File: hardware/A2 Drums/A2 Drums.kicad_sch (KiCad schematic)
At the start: 21 parts, among them T1 2N3904

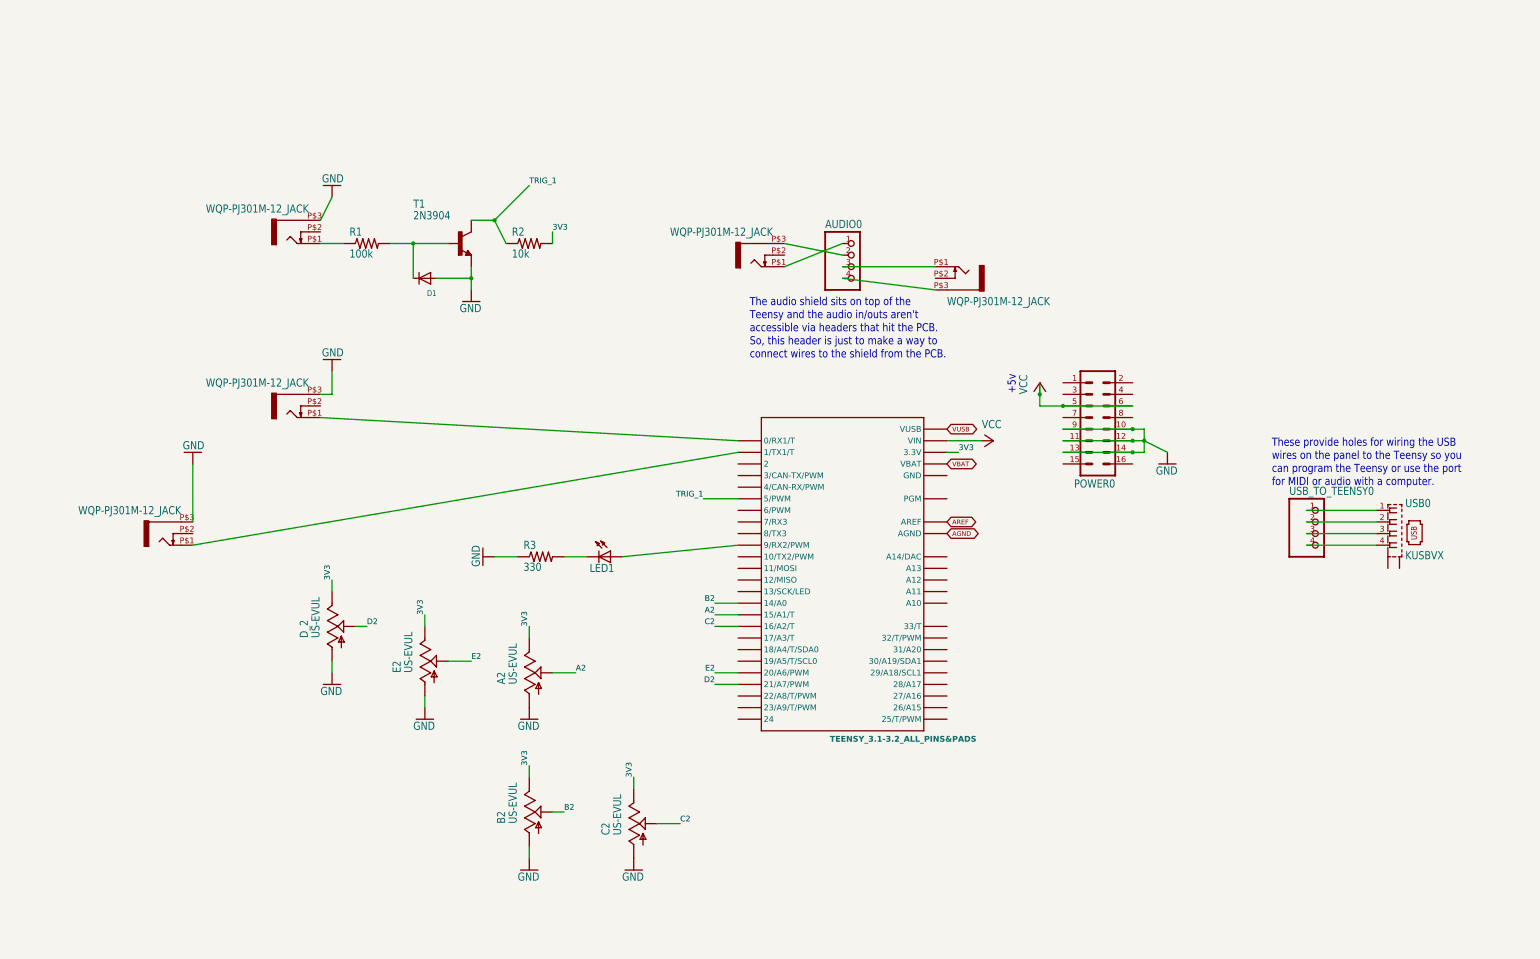
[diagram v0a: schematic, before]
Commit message: V2 of hardware and made a version of the software that uses the pt8211 chip for audio
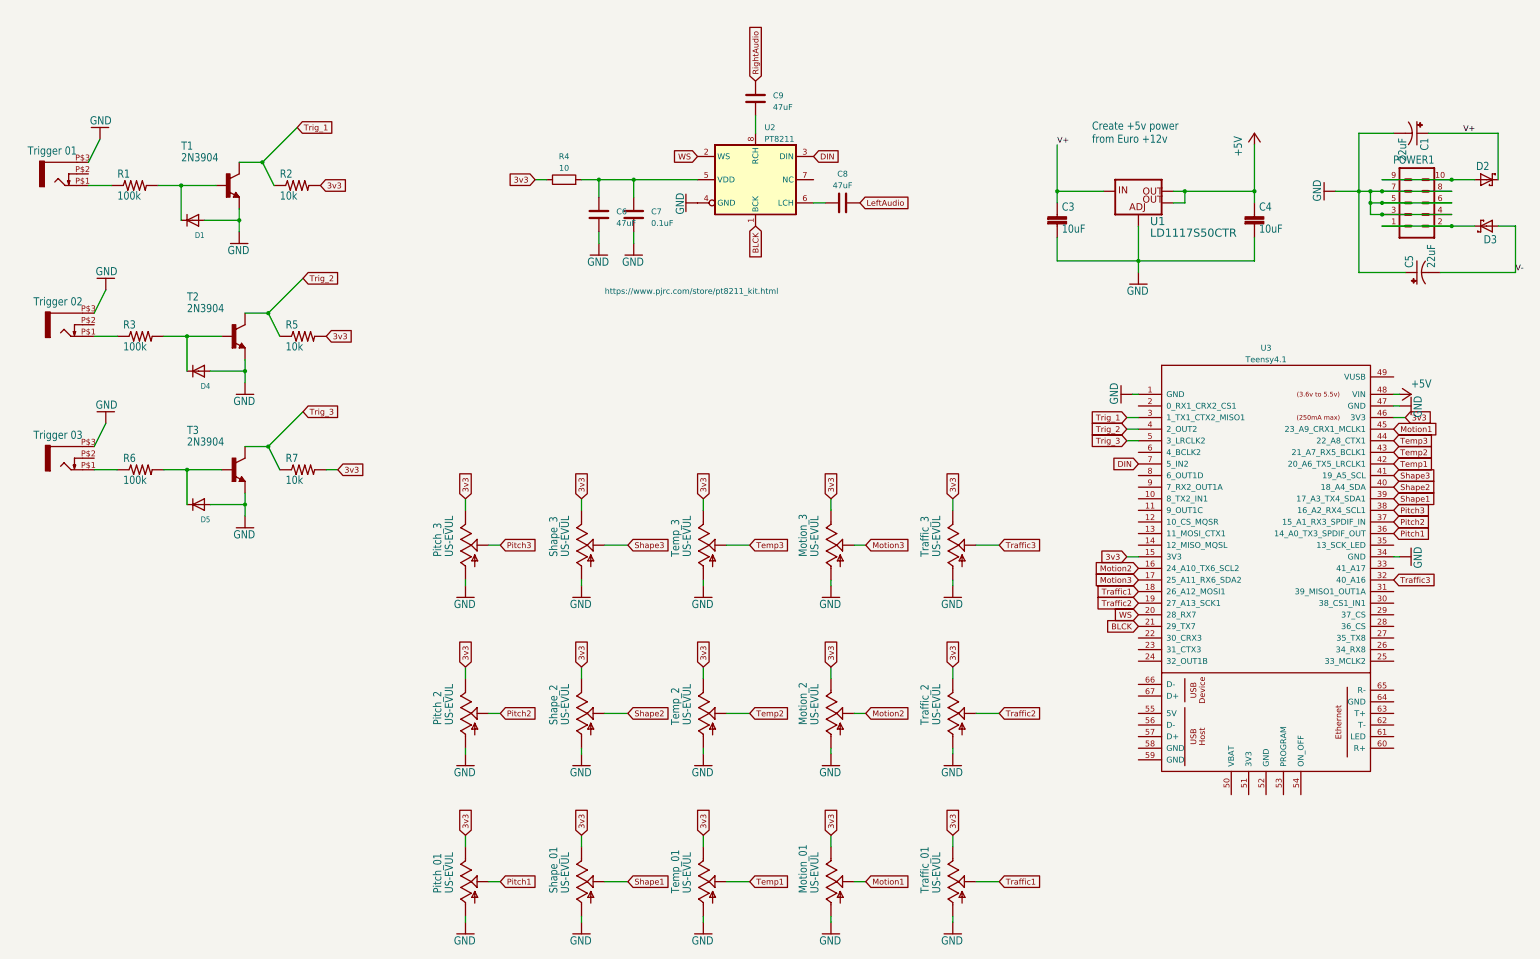
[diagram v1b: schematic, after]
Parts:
- removed AUDIO0, USB_TO_TEENSY0: PINHD-1X4, A2 Drums:1X04, symbol A2 Drums-eagle-import:PINHD-1X4
- removed AUD_IN_R0, AUD_OUT0, CD_IN0, CD_OUT0: WQP-PJ301M-12_JACK, A2 Drums:WQP-PJ301M-12_JACK, symbol A2 Drums-eagle-import:WQP-PJ301M-12_JACK
- removed LED1: LED3MM, A2 Drums:LED3MM, symbol A2 Drums-eagle-import:LED3MM
- removed POWER0: MA08-2, A2 Drums:MA08-2, symbol A2 Drums-eagle-import:MA08-2
- removed TEENSY_3.2: TEENSY_3.1-3.2_ALL_PINS&PADS, A2 Drums:TEENSY_3.0-3.2_ALL_PINS_&_PADS, symbol A2 Drums-eagle-import:TEENSY_3.1-3.2_ALL_PINS&PADS
- removed USB0: KUSBVX, A2 Drums:KUSBVX, symbol A2 Drums-eagle-import:KUSBVX
- added C1, C5: 22uF, Simple Euclidean PCB v4:E2,5-5, symbol Simple Euclidean PCB v4-eagle-import:CPOL-USE2.5-5
- added C3, C4: 10uF, Simple Euclidean PCB v4:C5B2.5, symbol Simple Euclidean PCB v4-eagle-import:C5/2.5
- added C6, C8, C9: 47uF, Capacitor_THT:C_Axial_L5.1mm_D3.1mm_P7.50mm_Horizontal, symbol Device:C
- added C7: 0.1uF, Capacitor_THT:C_Axial_L5.1mm_D3.1mm_P7.50mm_Horizontal, symbol Device:C
- added D2, D3: SCHOTTKY-DIODEDO41, Simple Euclidean PCB v4:DO41-10, symbol Simple Euclidean PCB v4-eagle-import:SCHOTTKY-DIODEDO41
- added D4, D5: DIODESOD-123, A2 Drums:SOD-123, symbol A2 Drums-eagle-import:DIODESOD-123
- added Motion_2, Motion_3, Pitch_2, Pitch_3, Shape_2, Shape_3, Temp_2, Temp_3, Traffic_2, Traffic_3: US-EVUL, A2 Drums:EVUFXL, symbol A2 Drums-eagle-import:US-EVUL
- added POWER1: MA05-2, Simple Euclidean PCB v4:MA05-2, symbol Simple Euclidean PCB v4-eagle-import:MA05-2
- added R4: 10, PCM_4ms_Resistor:R_Axial_DIN0207_L6.3mm_D2.5mm_P7.62mm_Horizontal, symbol Device:R
- added R5, R7: 10k, A2 Drums:R0805, symbol A2 Drums-eagle-import:R-US_R0805
- added R6: 100k, A2 Drums:R0805, symbol A2 Drums-eagle-import:R-US_R0805
- added T2, T3: 2N3904, A2 Drums:TO92, symbol A2 Drums-eagle-import:2N3904
- added TRIG2: Trigger 02, A2 Drums:WQP-PJ301M-12_JACK, symbol A2 Drums-eagle-import:WQP-PJ301M-12_JACK
- added TRIG3: Trigger 03, A2 Drums:WQP-PJ301M-12_JACK, symbol A2 Drums-eagle-import:WQP-PJ301M-12_JACK
- added U1: LD1117S50CTR, Simple Euclidean PCB v4:SOT223, symbol Simple Euclidean PCB v4-eagle-import:V_REG_LM1117SOT223
- added U2: PT8211, Package_SO:VSSOP-8_3.0x3.0mm_P0.65mm, symbol Timer:TLC555xPS
- added U3: Teensy4.1, symbol teensy:Teensy4.1
- R3: value 330 -> 100k
- TRIG1: value WQP-PJ301M-12_JACK -> Trigger 01
- renumbered B2 to Motion_01, D_2 to Pitch_01, E2 to Shape_01, A2 to Temp_01, C2 to Traffic_01
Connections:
- net GND: now also C1.-, C3.2, C4.2, C5.+, C6.2, C7.2, D4.A, D5.A, Motion_2.1 (A), Motion_3.1 (A), POWER1.3, POWER1.4, POWER1.5, POWER1.6, POWER1.7, POWER1.8, Pitch_2.1 (A), Pitch_3.1 (A), Shape_2.1 (A), Shape_3.1 (A), T2.3 (E), T3.3 (E), TRIG2.P$3 (1), TRIG3.P$3 (1), Temp_2.1 (A), Temp_3.1 (A), Traffic_2.1 (A), Traffic_3.1 (A), U1.1 (ADJ), U2.4 (GND), U3.1 (GND), U3.34 (GND), U3.47 (GND); no longer R3.1
- net at R3.2: now also D4.C, T2.2 (B)
- net 3V3 renamed 3v3
- net 3v3: now also Motion_2.3 (E), Motion_3.3 (E), Pitch_2.3 (E), Pitch_3.3 (E), R4.1, R5.2, R7.2, Shape_2.3 (E), Shape_3.3 (E), Temp_2.3 (E), Temp_3.3 (E), Traffic_2.3 (E), Traffic_3.3 (E), U3.15 (3V3), U3.46 (3V3)
- net A2 renamed Temp1
- net Temp1: now also U3.42 (20_A6_TX5_LRCLK1)
- net B2 renamed Motion1
- net Motion1: now also U3.45 (23_A9_CRX1_MCLK1)
- net C2 renamed Traffic1
- net Traffic1: now also U3.18 (26_A12_MOSI1)
- net D2 renamed Pitch1
- net Pitch1: now also U3.36 (14_A0_TX3_SPDIF_OUT)
- net E2 renamed Shape1
- net Shape1: now also U3.39 (17_A3_TX4_SDA1)
- net TRIG_1 renamed Trig_1
- net Trig_1: now also U3.3 (1_TX1_CTX2_MISO1)
- new net: C8.1, U2.6 (LCH)
- new net: R6.1, TRIG3.P$1 (2)
- new net: C6.1, C7.1, R4.2, U2.5 (VDD)
- new net: C9.1, U2.8 (RCH)
- new net: D5.C, R6.2, T3.2 (B)
- new net: R3.1, TRIG2.P$1 (2)
- new net: D2.A, POWER1.10, POWER1.9
- new net: D3.C, POWER1.1, POWER1.2
- new net +5V: C4.1, U1.2 (OUT), U1.4 (OUT@1), U3.48 (VIN)
- new net BLCK: U2.1 (BCK), U3.21 (29_TX7)
- new net DIN: U2.3 (DIN), U3.7 (5_IN2)
- new net LeftAudio: C8.2
- new net Motion2: Motion_2.2 (S), U3.16 (24_A10_TX6_SCL2)
- new net Motion3: Motion_3.2 (S), U3.17 (25_A11_RX6_SDA2)
- new net Pitch2: Pitch_2.2 (S), U3.37 (15_A1_RX3_SPDIF_IN)
- new net Pitch3: Pitch_3.2 (S), U3.38 (16_A2_RX4_SCL1)
- new net RightAudio: C9.2
- new net Shape2: Shape_2.2 (S), U3.40 (18_A4_SDA)
- new net Shape3: Shape_3.2 (S), U3.41 (19_A5_SCL)
- new net Temp2: Temp_2.2 (S), U3.43 (21_A7_RX5_BCLK1)
- new net Temp3: Temp_3.2 (S), U3.44 (22_A8_CTX1)
- new net Traffic2: Traffic_2.2 (S), U3.19 (27_A13_SCK1)
- new net Traffic3: Traffic_3.2 (S), U3.32 (40_A16)
- new net Trig_2: R5.1, T2.1 (C), U3.4 (2_OUT2)
- new net Trig_3: R7.1, T3.1 (C), U3.5 (3_LRCLK2)
- new net V+: C1.+, C3.1, D2.C, U1.3 (IN)
- new net V-: C5.-, D3.A
- new net WS: U2.2 (WS), U3.20 (28_RX7)
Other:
- note added: "Create +5v power from Euro +12v"
- note added: "https://www.pjrc.com/store/pt8211_kit.html"
- note removed: "+5v"
- note removed: "The audio shield sits on top of the Teensy and the audio in/outs aren't accessible via headers that hit the PCB. So, this header is just to make a way to connect wires to the shield from the PCB."
- note removed: "These provide holes for wiring the USB wires on the panel to the Teensy so you can program the Teensy or use the port for MIDI or audio with a computer."
- moved on the sheet: D1, Motion_01, Pitch_01, R1, R2, Shape_01, T1, Temp_01, Traffic_01
